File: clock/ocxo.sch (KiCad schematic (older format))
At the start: 44 parts, among them Q201 MMBT3904, U201 PCA9306, U202 DAC8830, U203 LMV722, U204 LTC2990, U205 LP3853, U206 NC7SZ125, U207 NC7SZ125, Y201 FVXO-HC53, Y202 CX210

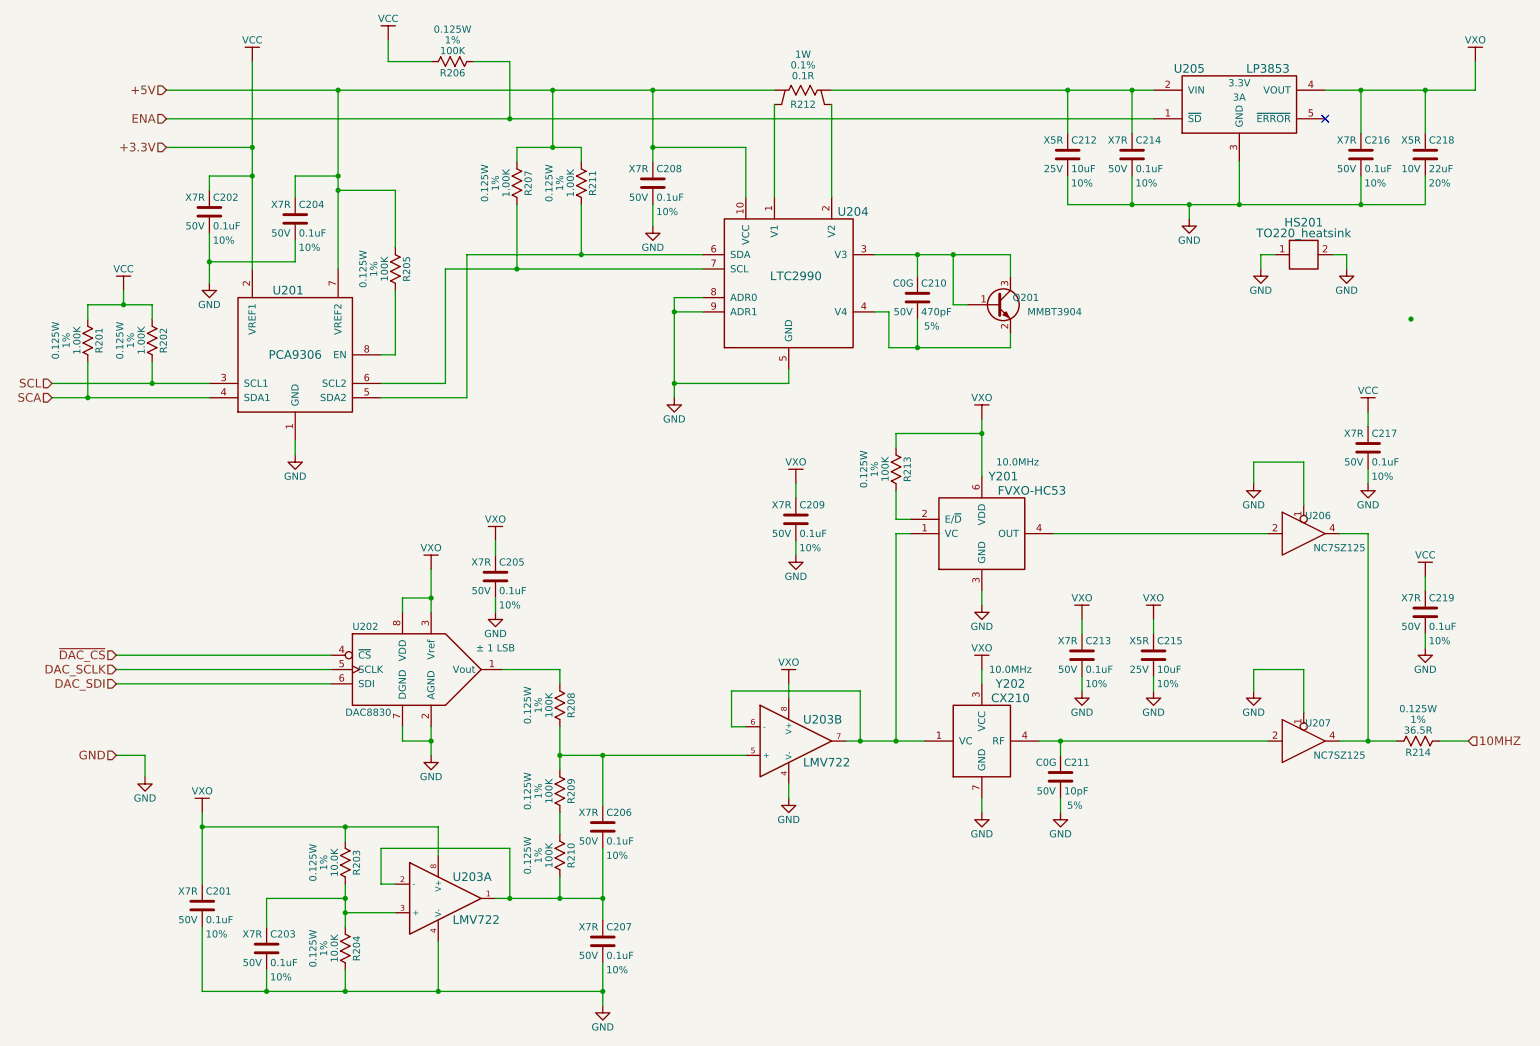
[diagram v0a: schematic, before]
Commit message: Add net names to most of the nets.
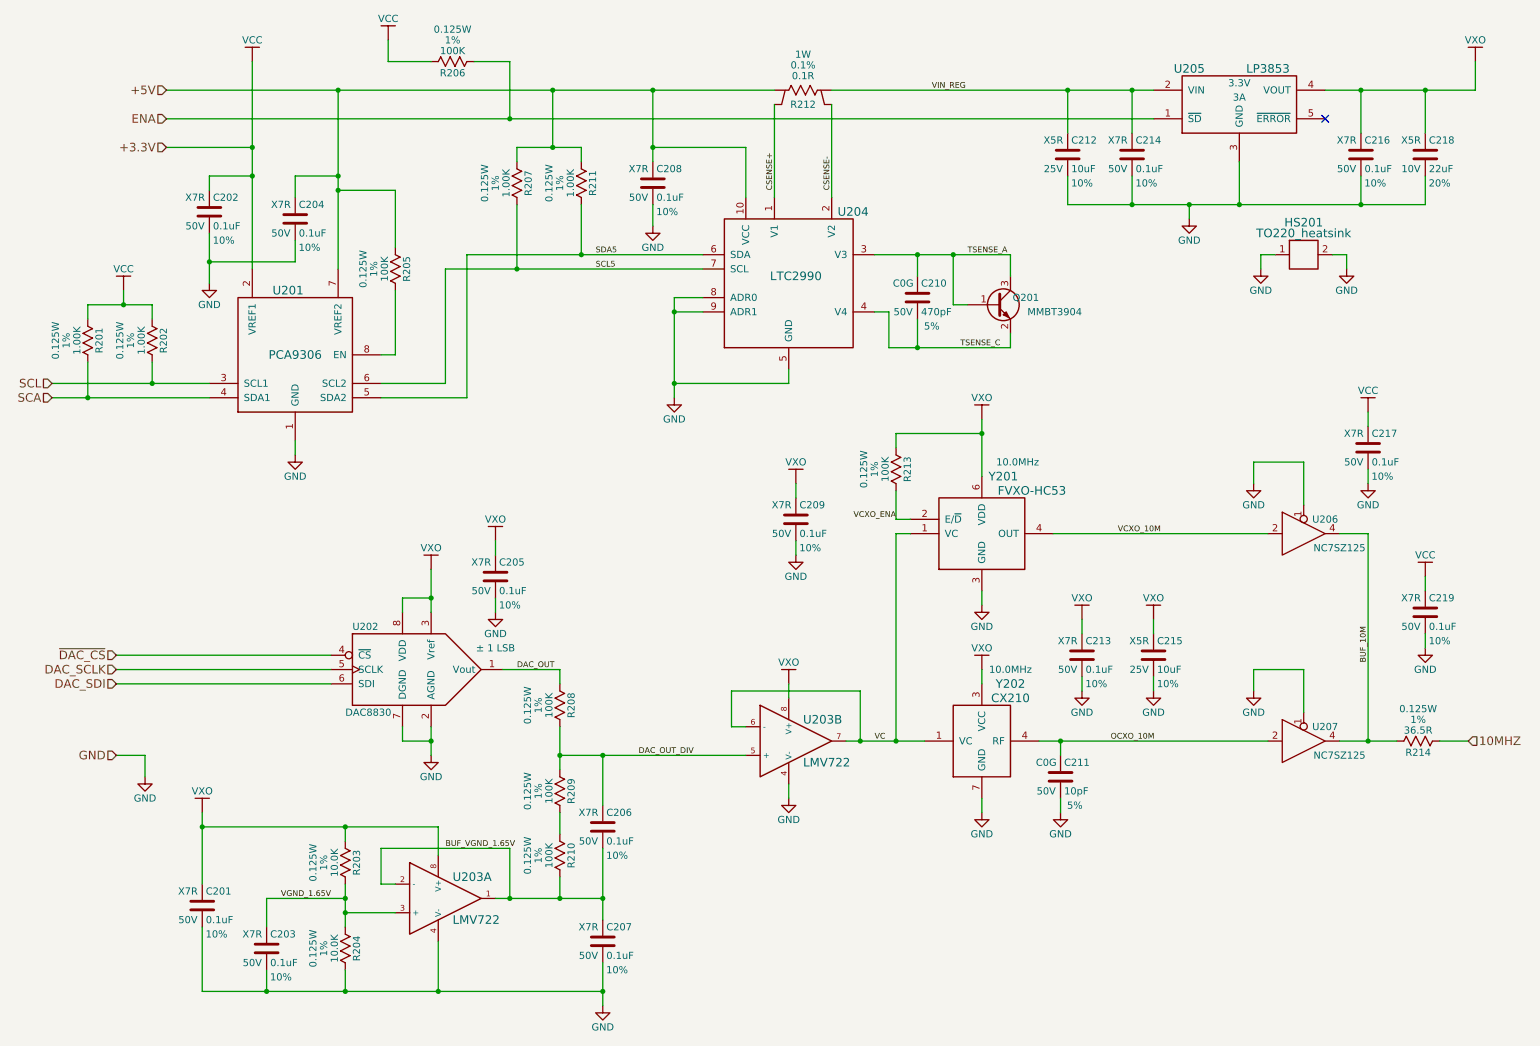
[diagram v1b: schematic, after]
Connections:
- net TSENSE_A: now reaches C210.1, Q201.1 (B), Q201.3 (C), U204.3 (V3)
- net TSENSE_C: now reaches C210.2, Q201.2 (E), U204.4 (V4)
- net VIN_REG: now reaches C212.1, C214.1, R212.1, U205.2 (VIN)
- net CSENSE-: now reaches R212.3, U204.2 (V2)
- net CSENSE+: now reaches R212.4, U204.1 (V1)
- net VGND_1.65V: now reaches C203.1, R203.2, R204.1, U203.3 (+)
- net BUF_VGND_1.65V: now reaches C206.2, C207.1, R210.2, U203.1, U203.2 (-)
- net DAC_OUT_DIV: now reaches C206.1, R208.2, R209.1, U203.5 (+)
- net DAC_OUT: now reaches R208.1, U202.1 (Vout)
- net VCXO_ENA: now reaches R213.2, Y201.2 (E/~D~)
- net SDA5: now reaches R211.2, U201.5 (SDA2), U204.6 (SDA)
- net SCL5: now reaches R207.2, U201.6 (SCL2), U204.7 (SCL)
- net VC: now reaches U203.6 (-), U203.7, Y201.1 (VC), Y202.1 (VC)
- net OCXO_10M: now reaches C211.1, U207.2, Y202.4 (RF)
- net VCXO_10M: now reaches U206.2, Y201.4 (OUT)
- net BUF_10M: now reaches R214.2, U206.4, U207.4
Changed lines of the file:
@@
 U 1 1 56373C66
 P 9600 4250
-F 0 "U206" H 9700 4375 50  0000 C CNN
+F 0 "U206" H 9750 4350 50  0000 C CNN
 F 1 "NC7SZ125" H 9850 4150 50  0000 C CNN
 F 2 "local:SOT-23-5_1.6x2.9mm_Pitch0.95mm" H 9350 4350 50  0001 C CNN
@@
 U 1 1 56373D10
 P 9600 5700
-F 0 "U207" H 9700 5825 50  0000 C CNN
+F 0 "U207" H 9750 5800 50  0000 C CNN
 F 1 "NC7SZ125" H 9850 5600 50  0000 C CNN
 F 2 "local:SOT-23-5_1.6x2.9mm_Pitch0.95mm" H 9350 5800 50  0001 C CNN
@@
 Connection ~ 4050 1350
 Connection ~ 4350 1150
-Connection ~ 10350 2750
 $Comp
 L CX210 Y202
@@
 	1    0    0    -1
 $EndComp
+Text Label 2450 6800 0    40   ~ 0
+VGND_1.65V
+Text Label 3600 6450 0    40   ~ 0
+BUF_VGND_1.65V
+Text Label 4950 5800 0    40   ~ 0
+DAC_OUT_DIV
+Text Label 4100 5200 0    40   ~ 0
+DAC_OUT
+Text Label 6600 5700 0    40   ~ 0
+VC
+Text Label 4650 2300 0    40   ~ 0
+SDA5
+Text Label 4650 2400 0    40   ~ 0
+SCL5
+Text Label 5900 1850 1    40   ~ 0
+CSENSE+
+Text Label 6300 1850 1    40   ~ 0
+CSENSE-
+Text Label 7250 2300 0    40   ~ 0
+TSENSE_A
+Text Label 7200 2950 0    40   ~ 0
+TSENSE_C
+Text Label 8250 5700 0    40   ~ 0
+OCXO_10M
+Text Label 8300 4250 0    40   ~ 0
+VCXO_10M
+Text Label 10050 5150 1    40   ~ 0
+BUF_10M
+Text Label 6750 4150 2    40   ~ 0
+VCXO_ENA
+Text Label 7000 1150 0    40   ~ 0
+VIN_REG
 $EndSCHEMATC

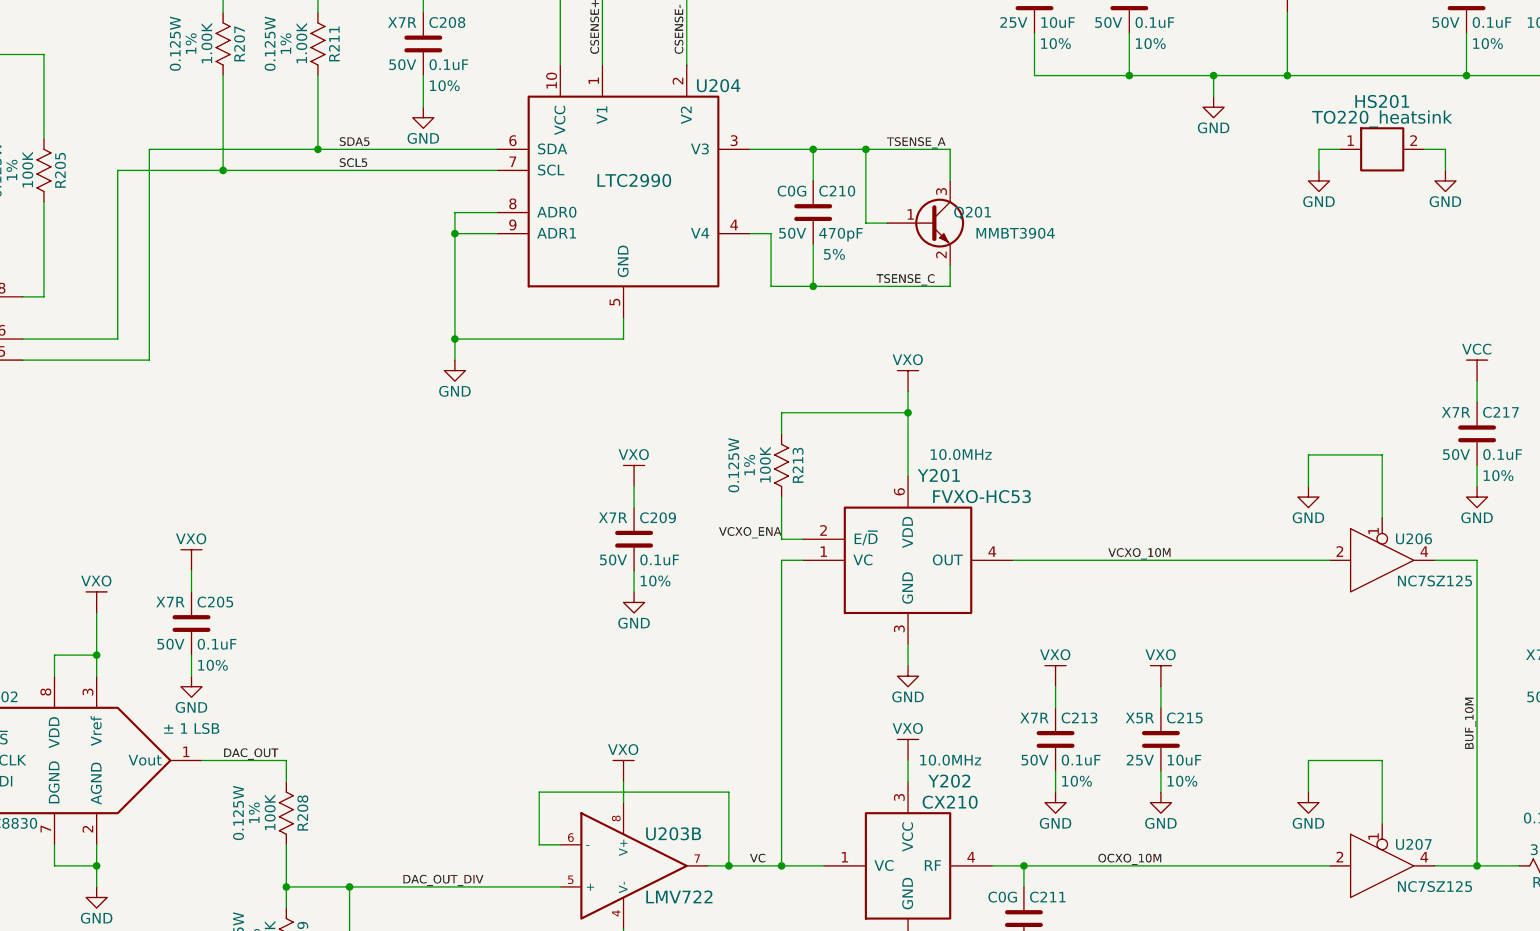
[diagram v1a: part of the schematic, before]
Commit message: Add filter for OCXO power.
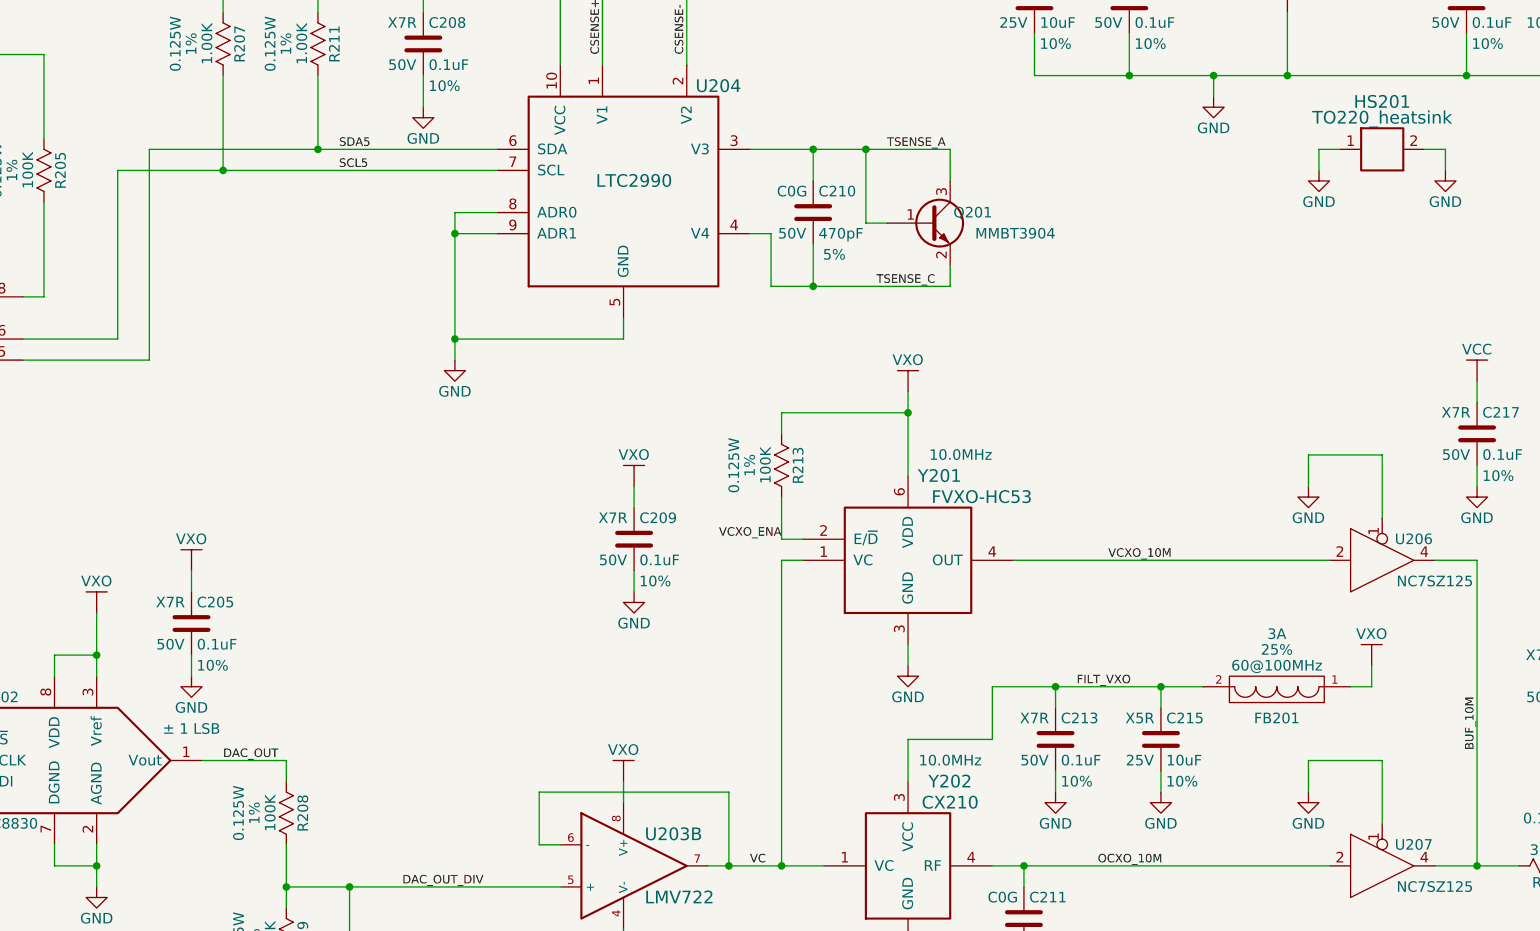
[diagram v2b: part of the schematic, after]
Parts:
- added FB201: 60@100MHz, Resistors_SMD:R_0805_HandSoldering, symbol FILTER
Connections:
- net VXO: now also FB201.1; no longer C213.1, C215.1, Y202.3 (VCC)
- new net FILT_VXO: C213.1, C215.1, FB201.2, Y202.3 (VCC)
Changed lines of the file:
@@
 $Comp
 L VXO #PWR024
-U 1 1 56248009
-P 8050 4850
-F 0 "#PWR024" H 8050 4700 50  0001 C CNN
-F 1 "VXO" H 8050 5000 50  0000 C CNN
-F 2 "" H 8050 4850 60  0000 C CNN
-F 3 "" H 8050 4850 60  0000 C CNN
-	1    8050 4850
-	1    0    0    -1
-$EndComp
-$Comp
-L VXO #PWR025
-U 1 1 56248194
-P 7350 5200
-F 0 "#PWR025" H 7350 5050 50  0001 C CNN
-F 1 "VXO" H 7350 5350 50  0000 C CNN
-F 2 "" H 7350 5200 60  0000 C CNN
-F 3 "" H 7350 5200 60  0000 C CNN
-	1    7350 5200
-	1    0    0    -1
-$EndComp
-$Comp
-L VXO #PWR026
 U 1 1 5624821F
 P 7350 3450
-F 0 "#PWR026" H 7350 3300 50  0001 C CNN
+F 0 "#PWR024" H 7350 3300 50  0001 C CNN
 F 1 "VXO" H 7350 3600 50  0000 C CNN
 F 2 "" H 7350 3450 60  0000 C CNN
@@
 $EndComp
 $Comp
-L VXO #PWR027
+L VXO #PWR025
 U 1 1 562483EB
 P 6000 5300
-F 0 "#PWR027" H 6000 5150 50  0001 C CNN
+F 0 "#PWR025" H 6000 5150 50  0001 C CNN
 F 1 "VXO" H 6000 5450 50  0000 C CNN
 F 2 "" H 6000 5300 60  0000 C CNN
@@
 $EndComp
 $Comp
-L VXO #PWR028
+L VXO #PWR026
 U 1 1 562484D6
 P 3500 4500
-F 0 "#PWR028" H 3500 4350 50  0001 C CNN
+F 0 "#PWR026" H 3500 4350 50  0001 C CNN
 F 1 "VXO" H 3500 4650 50  0000 C CNN
 F 2 "" H 3500 4500 60  0000 C CNN
@@
 $EndComp
 $Comp
-L VXO #PWR029
+L VXO #PWR027
 U 1 1 56248541
 P 3950 4300
-F 0 "#PWR029" H 3950 4150 50  0001 C CNN
+F 0 "#PWR027" H 3950 4150 50  0001 C CNN
 F 1 "VXO" H 3950 4450 50  0000 C CNN
 F 2 "" H 3950 4300 60  0000 C CNN
@@
 $EndComp
 $Comp
-L VXO #PWR030
+L VXO #PWR028
 U 1 1 56248C4D
 P 1900 6200
-F 0 "#PWR030" H 1900 6050 50  0001 C CNN
+F 0 "#PWR028" H 1900 6050 50  0001 C CNN
 F 1 "VXO" H 1900 6350 50  0000 C CNN
 F 2 "" H 1900 6200 60  0000 C CNN
@@
 $EndComp
 $Comp
-L GND #PWR031
+L GND #PWR029
 U 1 1 5624901D
 P 1500 5950
-F 0 "#PWR031" H 1500 5700 50  0001 C CNN
+F 0 "#PWR029" H 1500 5700 50  0001 C CNN
 F 1 "GND" H 1500 5800 50  0000 C CNN
 F 2 "" H 1500 5950 60  0000 C CNN
@@
 	3600 2400 5400 2400
 Wire Wire Line
-	5400 2300 3750 2300
+	3750 2300 5400 2300
 Wire Wire Line
 	3750 2300 3750 3300
@@
 	7350 3450 7350 3850
 Wire Wire Line
-	7350 5300 7350 5200
+	7350 5300 7350 5100
 Wire Wire Line
 	6000 5400 6000 5400
@@
 $EndComp
 $Comp
-L GND #PWR032
+L GND #PWR030
 U 1 1 56356688
 P 9300 2400
-F 0 "#PWR032" H 9300 2150 50  0001 C CNN
+F 0 "#PWR030" H 9300 2150 50  0001 C CNN
 F 1 "GND" H 9300 2250 50  0000 C CNN
 F 2 "" H 9300 2400 60  0000 C CNN
@@
 $EndComp
 $Comp
-L GND #PWR033
+L GND #PWR031
 U 1 1 563568AD
 P 9900 2400
-F 0 "#PWR033" H 9900 2150 50  0001 C CNN
+F 0 "#PWR031" H 9900 2150 50  0001 C CNN
 F 1 "GND" H 9900 2250 50  0000 C CNN
 F 2 "" H 9900 2400 60  0000 C CNN
@@
 	9300 2300 9300 2400
 $Comp
-L GND #PWR034
+L GND #PWR032
 U 1 1 5636F400
 P 7900 6200
-F 0 "#PWR034" H 7900 5950 50  0001 C CNN
+F 0 "#PWR032" H 7900 5950 50  0001 C CNN
 F 1 "GND" H 7900 6050 50  0000 C CNN
 F 2 "" H 7900 6200 60  0000 C CNN
@@
 $EndComp
 $Comp
-L VXO #PWR035
-U 1 1 563706F2
-P 8550 4850
-F 0 "#PWR035" H 8550 4700 50  0001 C CNN
-F 1 "VXO" H 8550 5000 50  0000 C CNN
-F 2 "" H 8550 4850 60  0000 C CNN
-F 3 "" H 8550 4850 60  0000 C CNN
-	1    8550 4850
-	1    0    0    -1
-$EndComp
-$Comp
-L GND #PWR036
+L GND #PWR033
 U 1 1 56370766
 P 8550 5350
-F 0 "#PWR036" H 8550 5100 50  0001 C CNN
+F 0 "#PWR033" H 8550 5100 50  0001 C CNN
 F 1 "GND" H 8550 5200 50  0000 C CNN
 F 2 "" H 8550 5350 60  0000 C CNN
@@
 	8550 5350 8550 5250
 Wire Wire Line
-	8550 4950 8550 4850
+	8550 4850 8550 4950
 Wire Wire Line
 	7750 5700 9350 5700
@@
 	9850 5700 10250 5700
 $Comp
-L VCC #PWR037
+L VCC #PWR034
 U 1 1 563724DA
 P 10450 4550
-F 0 "#PWR037" H 10450 4400 50  0001 C CNN
+F 0 "#PWR034" H 10450 4400 50  0001 C CNN
 F 1 "VCC" H 10450 4700 50  0000 C CNN
 F 2 "" H 10450 4550 60  0000 C CNN
@@
 $EndComp
 $Comp
-L GND #PWR038
+L GND #PWR035
 U 1 1 56372768
 P 10450 5050
-F 0 "#PWR038" H 10450 4800 50  0001 C CNN
+F 0 "#PWR035" H 10450 4800 50  0001 C CNN
 F 1 "GND" H 10450 4900 50  0000 C CNN
 F 2 "" H 10450 5050 60  0000 C CNN
@@
 	10450 4550 10450 4650
 $Comp
-L GND #PWR039
+L GND #PWR036
 U 1 1 56372915
 P 9250 5350
-F 0 "#PWR039" H 9250 5100 50  0001 C CNN
+F 0 "#PWR036" H 9250 5100 50  0001 C CNN
 F 1 "GND" H 9250 5200 50  0000 C CNN
 F 2 "" H 9250 5350 60  0000 C CNN
@@
 	9250 5200 9250 5350
 $Comp
-L VCC #PWR040
+L VCC #PWR037
 U 1 1 56372BE4
 P 2250 950
-F 0 "#PWR040" H 2250 800 50  0001 C CNN
+F 0 "#PWR037" H 2250 800 50  0001 C CNN
 F 1 "VCC" H 2250 1100 50  0000 C CNN
 F 2 "" H 2250 950 60  0000 C CNN
@@
 	9850 4250 10050 4250
 $Comp
-L GND #PWR041
+L GND #PWR038
 U 1 1 563736D6
 P 9250 3900
-F 0 "#PWR041" H 9250 3650 50  0001 C CNN
+F 0 "#PWR038" H 9250 3650 50  0001 C CNN
 F 1 "GND" H 9250 3750 50  0000 C CNN
 F 2 "" H 9250 3900 60  0000 C CNN
@@
 $EndComp
 $Comp
-L VCC #PWR042
+L VCC #PWR039
 U 1 1 56373FA5
 P 10050 3400
-F 0 "#PWR042" H 10050 3250 50  0001 C CNN
+F 0 "#PWR039" H 10050 3250 50  0001 C CNN
 F 1 "VCC" H 10050 3550 50  0000 C CNN
 F 2 "" H 10050 3400 60  0000 C CNN
@@
 $EndComp
 $Comp
-L GND #PWR043
+L GND #PWR040
 U 1 1 56373FAB
 P 10050 3900
-F 0 "#PWR043" H 10050 3650 50  0001 C CNN
+F 0 "#PWR040" H 10050 3650 50  0001 C CNN
 F 1 "GND" H 10050 3750 50  0000 C CNN
 F 2 "" H 10050 3900 60  0000 C CNN
@@
 	1550 2650 1550 2750
 $Comp
-L VCC #PWR044
+L VCC #PWR041
 U 1 1 56383EBC
 P 1350 2550
-F 0 "#PWR044" H 1350 2400 50  0001 C CNN
+F 0 "#PWR041" H 1350 2400 50  0001 C CNN
 F 1 "VCC" H 1350 2700 50  0000 C CNN
 F 2 "" H 1350 2550 60  0000 C CNN
@@
 $EndComp
 $Comp
-L VCC #PWR045
+L VCC #PWR042
 U 1 1 56401757
 P 3200 800
-F 0 "#PWR045" H 3200 650 50  0001 C CNN
+F 0 "#PWR042" H 3200 650 50  0001 C CNN
 F 1 "VCC" H 3200 950 50  0000 C CNN
 F 2 "" H 3200 800 60  0000 C CNN
@@
 Text Label 7000 1150 0    40   ~ 0
 VIN_REG
+$Comp
+L FILTER FB201
+U 1 1 56416346
+P 9100 4850
+F 0 "FB201" H 9100 5000 50  0000 C CNN
+F 1 "60@100MHz" H 9100 4750 50  0000 C CNN
+F 2 "Resistors_SMD:R_0805_HandSoldering" H 9100 4850 60  0001 C CNN
+F 3 "" H 9100 4850 60  0000 C CNN
+F 4 "3A" H 9100 4600 50  0000 C CNN "Current"
+F 5 "25%" H 9100 4675 50  0000 C CNN "Tolerance"
+F 6 "Pulse Electronics" H 9100 4850 60  0001 C CNN "Manufacturer"
+F 7 "PE-0805PFB600ST" H 9100 4850 60  0001 C CNN "PartNum"
+	1    9100 4850
+	-1   0    0    1
+$EndComp
+Wire Wire Line
+	7350 5100 7750 5100
+Wire Wire Line
+	7750 5100 7750 4850
+Wire Wire Line
+	7750 4850 8750 4850
+Connection ~ 8050 4850
+Connection ~ 8550 4850
+$Comp
+L VXO #PWR043
+U 1 1 56416BAD
+P 9550 4750
+F 0 "#PWR043" H 9550 4600 50  0001 C CNN
+F 1 "VXO" H 9550 4900 50  0000 C CNN
+F 2 "" H 9550 4750 60  0000 C CNN
+F 3 "" H 9550 4750 60  0000 C CNN
+	1    9550 4750
+	1    0    0    -1
+$EndComp
+Wire Wire Line
+	9550 4750 9550 4850
+Wire Wire Line
+	9550 4850 9450 4850
+Text Label 8150 4850 0    40   ~ 0
+FILT_VXO
 $EndSCHEMATC
